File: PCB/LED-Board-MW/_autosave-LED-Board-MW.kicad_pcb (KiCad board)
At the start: 2 copper layers, 23 parts, among them T1 1755736, T2 1755736, T3 1755736, U1 TPS61165DBVR, U2 TPS61165DBVR

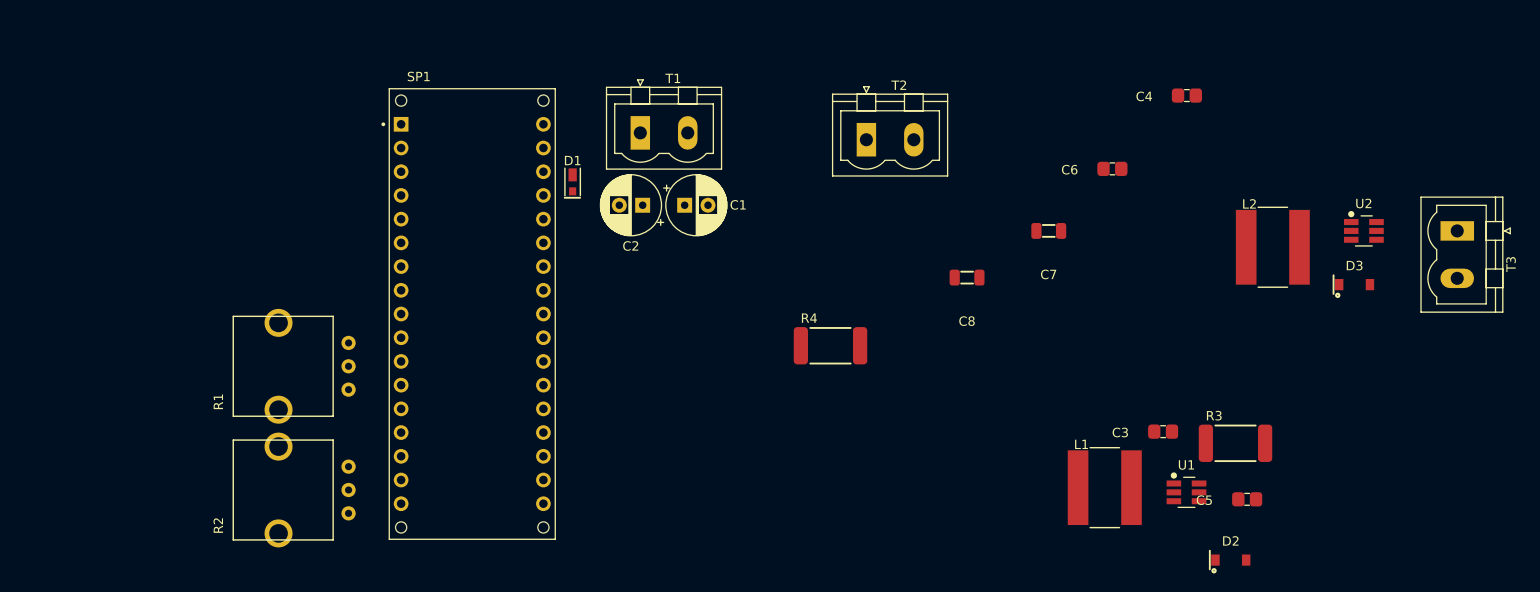
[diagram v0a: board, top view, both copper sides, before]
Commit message: Board Started
Started doing board based on schetaic, design make change since LEDs are huge
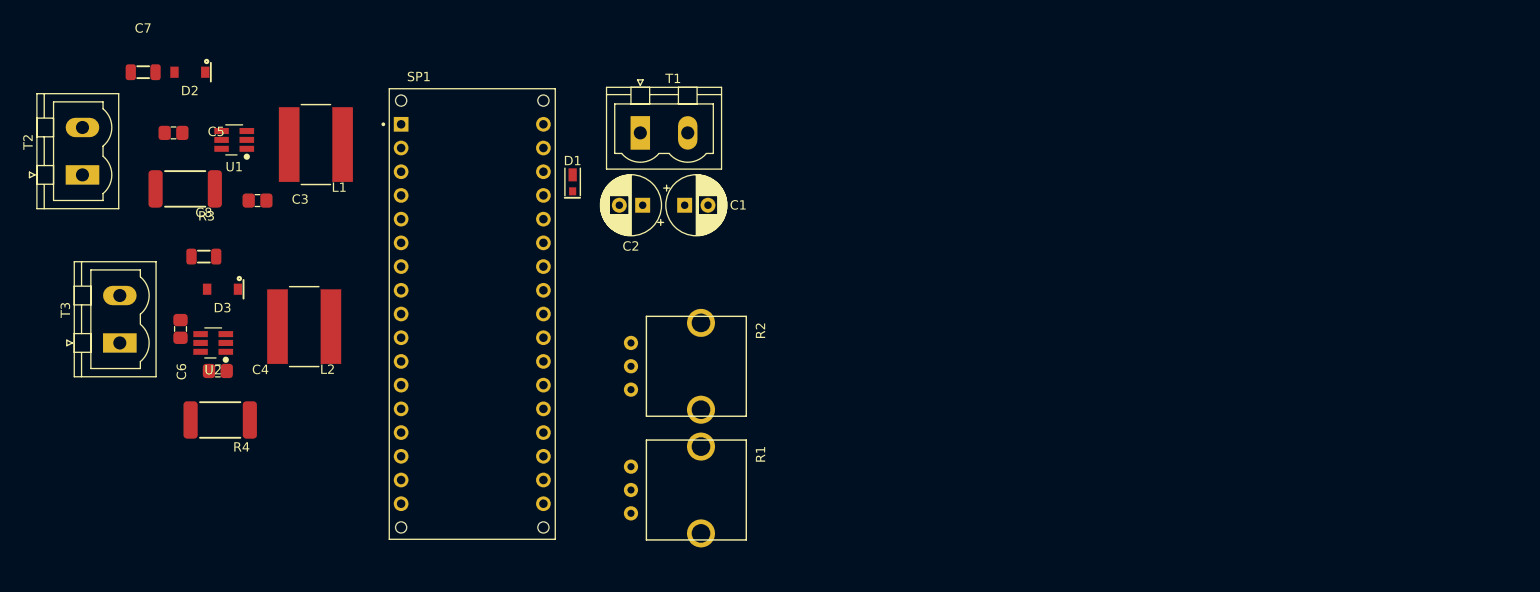
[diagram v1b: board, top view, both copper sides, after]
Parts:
- moved T3 143.8 mm to (70.8, 93.5), turned to 90 degrees
- moved U2 123.8 mm to (80.8, 93.5), turned to 180 degrees
- moved D2 123.1 mm to (78.2, 64.5), turned to 180 degrees
- moved C5 121.5 mm to (76.5, 71.0), turned to 180 degrees
- moved D3 121.3 mm to (81.8, 87.8), turned to 180 degrees
- moved R3 115.8 mm to (77.8, 77.0), turned to 180 degrees
- moved U1 108.8 mm to (83.0, 71.8), turned to 180 degrees
- moved C4 107.9 mm to (81.2, 96.5), turned to 180 degrees
- moved L2 104.1 mm to (90.5, 91.8), turned to 180 degrees
- moved C6 101.3 mm to (77.2, 92.0), turned to 90 degrees
- moved C3 100.1 mm to (85.5, 78.2), turned to 180 degrees
- moved C7 98.5 mm to (73.2, 64.5), turned to 180 degrees
- moved L1 92.1 mm to (91.8, 72.2), turned to 180 degrees
- moved T2 84.0 mm to (66.8, 75.5), turned to 90 degrees
- moved C8 81.8 mm to (79.8, 84.2), turned to 180 degrees
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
